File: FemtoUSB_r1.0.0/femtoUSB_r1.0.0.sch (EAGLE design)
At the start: 27 parts, among them IC1 ATSAMD21E18A-MUT

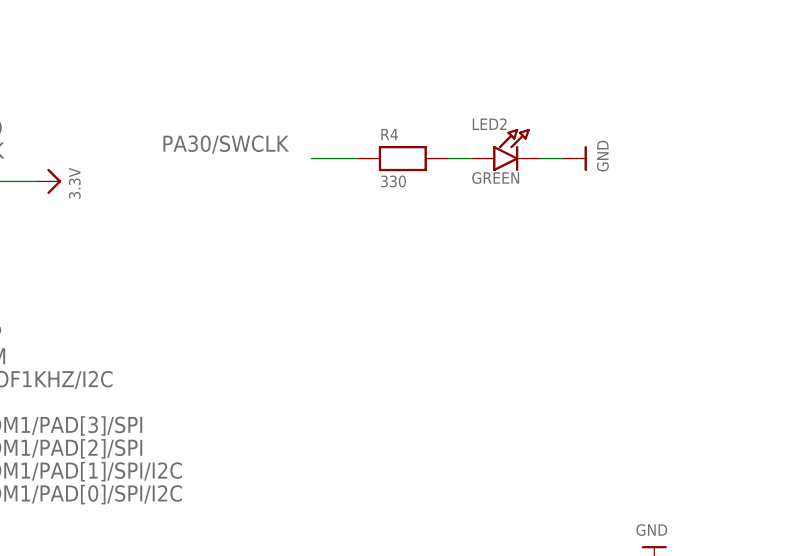
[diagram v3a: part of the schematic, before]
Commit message: Updating r1.x version of FemtoUSB (QFN and QFP chip version). Pin PA15 and GND pads now available to start board up in bootloader mode (SAM-BA)
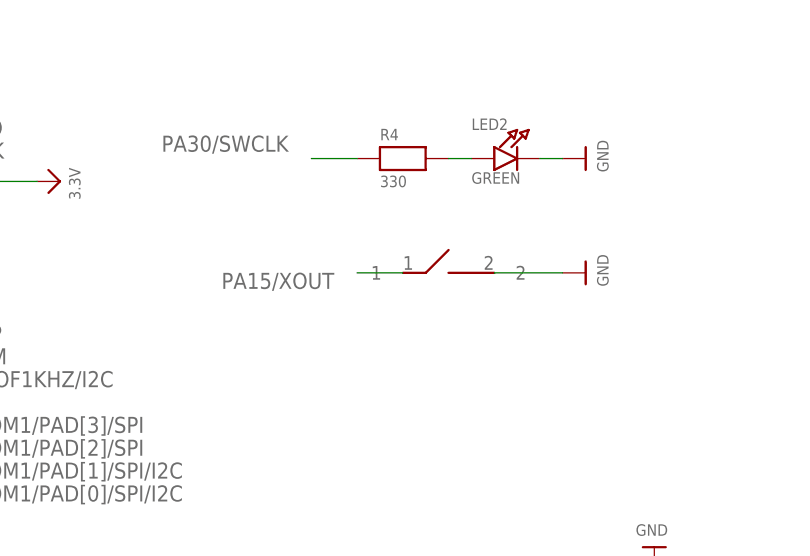
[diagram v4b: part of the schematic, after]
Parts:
- added U$38: SPST_SMD, femtoduino:SPST_SMD
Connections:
- net GND: now also U$38.2
- net PA15/XOUT: now also U$38.1
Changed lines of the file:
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@@
 <part name="U$37" library="microbuilder" deviceset="GND" device=""/>
 <part name="C8" library="microbuilder" deviceset="CAP_CERAMIC" device="_0402MP" value="10uF"/>
+<part name="U$38" library="femtoduino" deviceset="SPST_SMD" device=""/>
+<part name="U$39" library="microbuilder" deviceset="GND" device=""/>
 </parts>
 <sheets>
@@
 <instance part="U$37" gate="G$1" x="241.3" y="43.18"/>
 <instance part="C8" gate="G$1" x="241.3" y="58.42" rot="R180"/>
+<instance part="U$38" gate="G$1" x="160.02" y="152.4"/>
+<instance part="U$39" gate="G$1" x="172.72" y="152.4" rot="R90"/>
 </instances>
 <busses>
@@
 <label x="236.22" y="114.3" size="1.778" layer="95"/>
 </segment>
+<segment>
+<pinref part="U$38" gate="G$1" pin="1"/>
+<wire x1="152.4" y1="152.4" x2="147.32" y2="152.4" width="0.1524" layer="91"/>
+<label x="144.78" y="152.4" size="1.778" layer="95" rot="R180"/>
+</segment>
 </net>
 <net name="PA16/SERCOM1/PAD[0]/SPI/I2C" class="0">
@@
 <pinref part="C8" gate="G$1" pin="P$1"/>
 </segment>
-</net>
+<segment>
+<pinref part="U$38" gate="G$1" pin="2"/>
+<wire x1="162.56" y1="152.4" x2="170.18" y2="152.4" width="0.1524" layer="91"/>
+<pinref part="U$39" gate="G$1" pin="GND"/>
+</segment>
+</net>

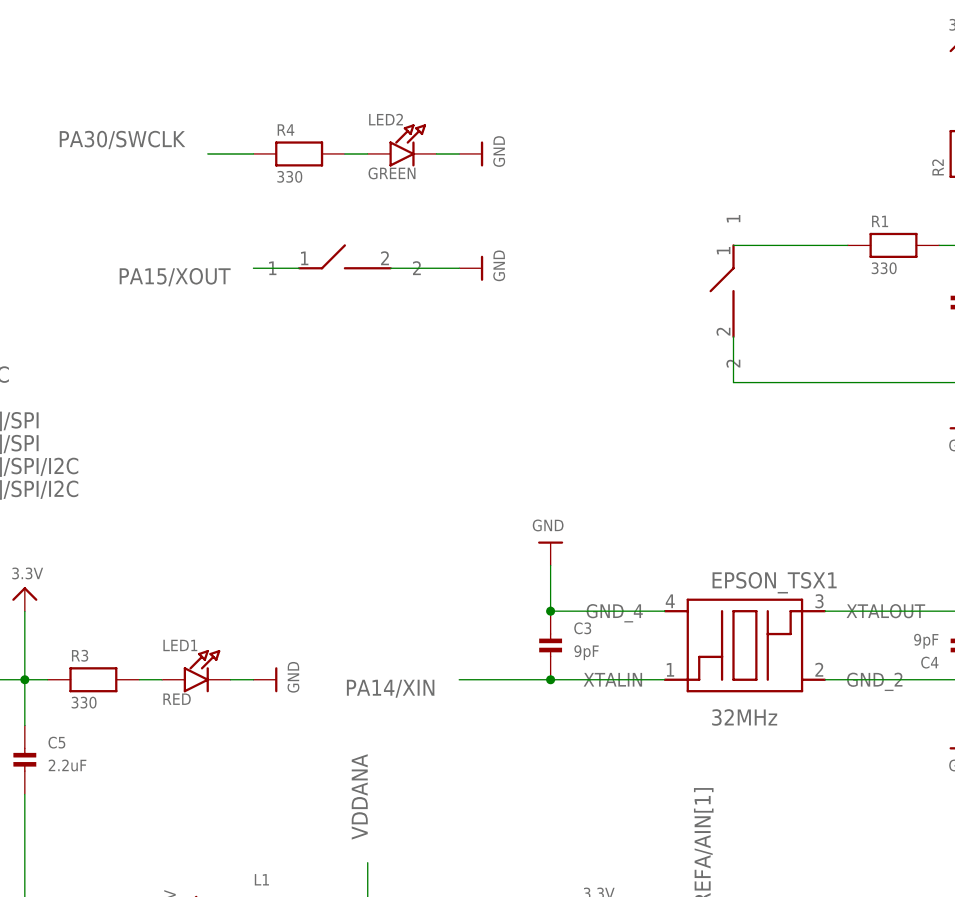
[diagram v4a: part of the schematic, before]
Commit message: Updating gerbers and BoM/Partslist of QFN version
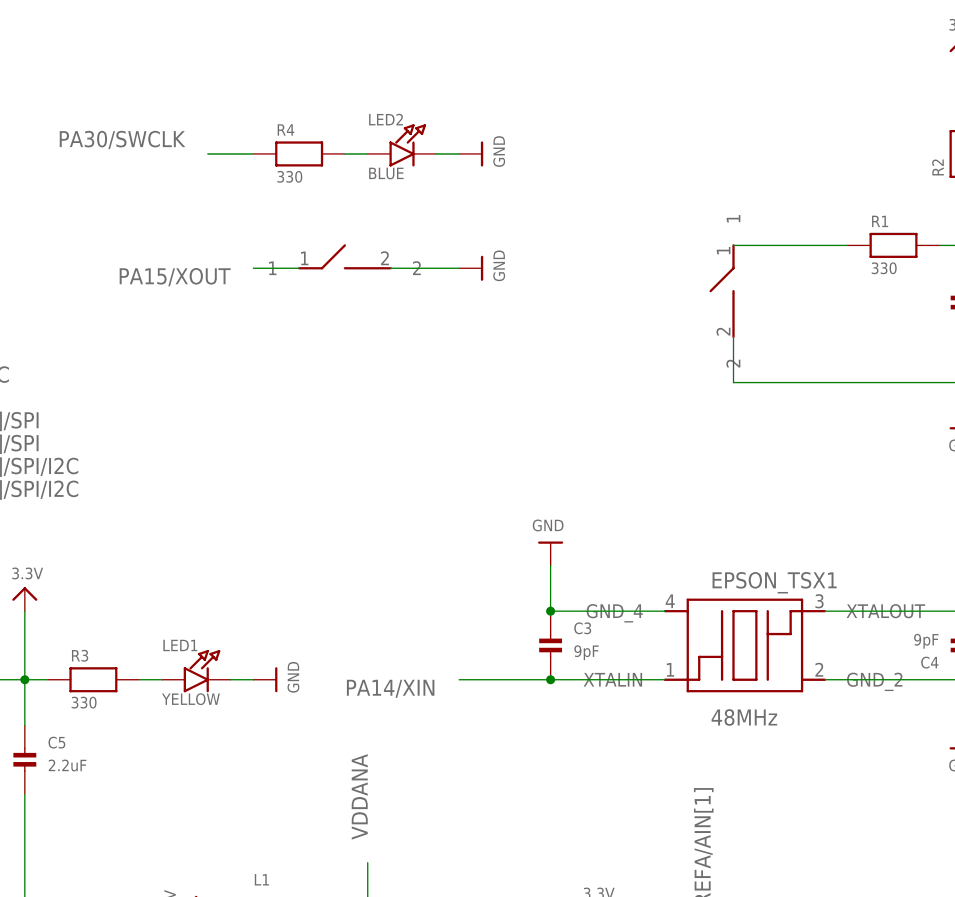
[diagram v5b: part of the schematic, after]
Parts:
- EPSON_TSX1: value 32MHz -> 48MHz
- LED1: value RED -> YELLOW
- LED2: value GREEN -> BLUE
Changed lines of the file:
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@@
 <grid distance="0.1" unitdist="inch" unit="inch" style="lines" multiple="1" display="no" altdistance="0.01" altunitdist="inch" altunit="inch"/>
 <layers>
-<layer number="1" name="Top" color="4" fill="1" visible="no" active="no"/>
-<layer number="2" name="Route2" color="1" fill="3" visible="no" active="no"/>
-<layer number="3" name="Route3" color="4" fill="3" visible="no" active="no"/>
-<layer number="14" name="Route14" color="1" fill="6" visible="no" active="no"/>
-<layer number="15" name="Route15" color="4" fill="6" visible="no" active="no"/>
-<layer number="16" name="Bottom" color="1" fill="1" visible="no" active="no"/>
-<layer number="17" name="Pads" color="2" fill="1" visible="no" active="no"/>
-<layer number="18" name="Vias" color="2" fill="1" visible="no" active="no"/>
-<layer number="19" name="Unrouted" color="6" fill="1" visible="no" active="no"/>
-<layer number="20" name="Dimension" color="15" fill="1" visible="no" active="no"/>
-<layer number="21" name="tPlace" color="7" fill="1" visible="no" active="no"/>
-<layer number="22" name="bPlace" color="7" fill="1" visible="no" active="no"/>
-<layer number="23" name="tOrigins" color="15" fill="1" visible="no" active="no"/>
-<layer number="24" name="bOrigins" color="15" fill="1" visible="no" active="no"/>
-<layer number="25" name="tNames" color="7" fill="1" visible="no" active="no"/>
-<layer number="26" name="bNames" color="7" fill="1" visible="no" active="no"/>
-<layer number="27" name="tValues" color="7" fill="1" visible="no" active="no"/>
-<layer number="28" name="bValues" color="7" fill="1" visible="no" active="no"/>
+<layer number="1" name="Top" color="4" fill="1" visible="yes" active="no"/>
+<layer number="2" name="Route2" color="1" fill="3" visible="yes" active="no"/>
+<layer number="3" name="Route3" color="4" fill="3" visible="yes" active="no"/>
+<layer number="14" name="Route14" color="1" fill="6" visible="yes" active="no"/>
+<layer number="15" name="Route15" color="4" fill="6" visible="yes" active="no"/>
+<layer number="16" name="Bottom" color="1" fill="1" visible="yes" active="no"/>
+<layer number="17" name="Pads" color="2" fill="1" visible="yes" active="no"/>
+<layer number="18" name="Vias" color="2" fill="1" visible="yes" active="no"/>
+<layer number="19" name="Unrouted" color="6" fill="1" visible="yes" active="no"/>
+<layer number="20" name="Dimension" color="15" fill="1" visible="yes" active="no"/>
+<layer number="21" name="tPlace" color="7" fill="1" visible="yes" active="no"/>
+<layer number="22" name="bPlace" color="7" fill="1" visible="yes" active="no"/>
+<layer number="23" name="tOrigins" color="15" fill="1" visible="yes" active="no"/>
+<layer number="24" name="bOrigins" color="15" fill="1" visible="yes" active="no"/>
+<layer number="25" name="tNames" color="7" fill="1" visible="yes" active="no"/>
+<layer number="26" name="bNames" color="7" fill="1" visible="yes" active="no"/>
+<layer number="27" name="tValues" color="7" fill="1" visible="yes" active="no"/>
+<layer number="28" name="bValues" color="7" fill="1" visible="yes" active="no"/>
 <layer number="29" name="tStop" color="7" fill="3" visible="no" active="no"/>
 <layer number="30" name="bStop" color="7" fill="6" visible="no" active="no"/>
@@
 <layer number="35" name="tGlue" color="7" fill="4" visible="no" active="no"/>
 <layer number="36" name="bGlue" color="7" fill="5" visible="no" active="no"/>
-<layer number="37" name="tTest" color="7" fill="1" visible="no" active="no"/>
-<layer number="38" name="bTest" color="7" fill="1" visible="no" active="no"/>
+<layer number="37" name="tTest" color="7" fill="1" visible="yes" active="no"/>
+<layer number="38" name="bTest" color="7" fill="1" visible="yes" active="no"/>
 <layer number="39" name="tKeepout" color="4" fill="11" visible="no" active="no"/>
 <layer number="40" name="bKeepout" color="1" fill="11" visible="no" active="no"/>
@@
 <layer number="44" name="Drills" color="7" fill="1" visible="no" active="no"/>
 <layer number="45" name="Holes" color="7" fill="1" visible="no" active="no"/>
-<layer number="46" name="Milling" color="3" fill="1" visible="no" active="no"/>
-<layer number="47" name="Measures" color="7" fill="1" visible="no" active="no"/>
-<layer number="48" name="Document" color="7" fill="1" visible="no" active="no"/>
-<layer number="49" name="Reference" color="7" fill="1" visible="no" active="no"/>
-<layer number="50" name="dxf" color="7" fill="1" visible="no" active="no"/>
-<layer number="51" name="tDocu" color="7" fill="1" visible="no" active="no"/>
-<layer number="52" name="bDocu" color="7" fill="1" visible="no" active="no"/>
-<layer number="53" name="tGND_GNDA" color="7" fill="9" visible="no" active="no"/>
-<layer number="54" name="bGND_GNDA" color="1" fill="9" visible="no" active="no"/>
-<layer number="56" name="wert" color="7" fill="1" visible="no" active="no"/>
+<layer number="46" name="Milling" color="3" fill="1" visible="yes" active="no"/>
+<layer number="47" name="Measures" color="7" fill="1" visible="yes" active="no"/>
+<layer number="48" name="Document" color="7" fill="1" visible="yes" active="no"/>
+<layer number="49" name="Reference" color="7" fill="1" visible="yes" active="no"/>
+<layer number="50" name="dxf" color="7" fill="1" visible="yes" active="no"/>
+<layer number="51" name="tDocu" color="7" fill="1" visible="yes" active="no"/>
+<layer number="52" name="bDocu" color="7" fill="1" visible="yes" active="no"/>
+<layer number="53" name="tGND_GNDA" color="7" fill="9" visible="yes" active="no"/>
+<layer number="54" name="bGND_GNDA" color="1" fill="9" visible="yes" active="no"/>
+<layer number="56" name="wert" color="7" fill="1" visible="yes" active="no"/>
 <layer number="91" name="Nets" color="2" fill="1" visible="yes" active="yes"/>
 <layer number="92" name="Busses" color="1" fill="1" visible="yes" active="yes"/>
@@
 <part name="FB1" library="microbuilder" deviceset="FERRITE" device="_0603MP"/>
 <part name="C1" library="microbuilder" deviceset="CAP_CERAMIC" device="_0402MP" value="0.1uF"/>
-<part name="LED1" library="microbuilder" deviceset="LED" device="0603_NOOUTLINE" value="RED"/>
+<part name="LED1" library="microbuilder" deviceset="LED" device="0603_NOOUTLINE" value="YELLOW"/>
 <part name="R1" library="microbuilder" deviceset="RESISTOR" device="_0402MP" value="330"/>
 <part name="C2" library="microbuilder" deviceset="CAP_CERAMIC" device="_0402MP" value="4.7uF"/>
 <part name="C3" library="microbuilder" deviceset="CAP_CERAMIC" device="_0402MP" value="9pF"/>
 <part name="C4" library="microbuilder" deviceset="CAP_CERAMIC" device="_0402MP" value="9pF"/>
-<part name="LED2" library="microbuilder" deviceset="LED" device="0603_NOOUTLINE" value="GREEN"/>
+<part name="LED2" library="microbuilder" deviceset="LED" device="0603_NOOUTLINE" value="BLUE"/>
 <part name="R2" library="microbuilder" deviceset="RESISTOR" device="_0402MP" value="10K"/>
 <part name="R3" library="microbuilder" deviceset="RESISTOR" device="_0402MP" value="330"/>
@@
 <part name="U$24" library="microbuilder" deviceset="GND" device=""/>
 <part name="U$25" library="microbuilder" deviceset="GND" device=""/>
-<part name="EPSON_TSX1" library="crystals" deviceset="TSX-3225" device="" value="32MHz">
+<part name="EPSON_TSX1" library="crystals" deviceset="TSX-3225" device="" value="48MHz">
 <attribute name="DIGIKEY_PART" value="TSX-3225 32.0000MF15X-B-ND"/>
 </part>
